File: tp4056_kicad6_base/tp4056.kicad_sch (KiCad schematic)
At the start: 21 parts, among them J1 USB_B_Micro, J2 Conn_01x01_Female, J3 Conn_01x01_Female, J4 Conn_01x01_Female, J5 Conn_01x01_Female, J6 Conn_01x01_Female, J7 Conn_01x01_Female, U1 TP4056, U2 DW01, U3 FS8205A

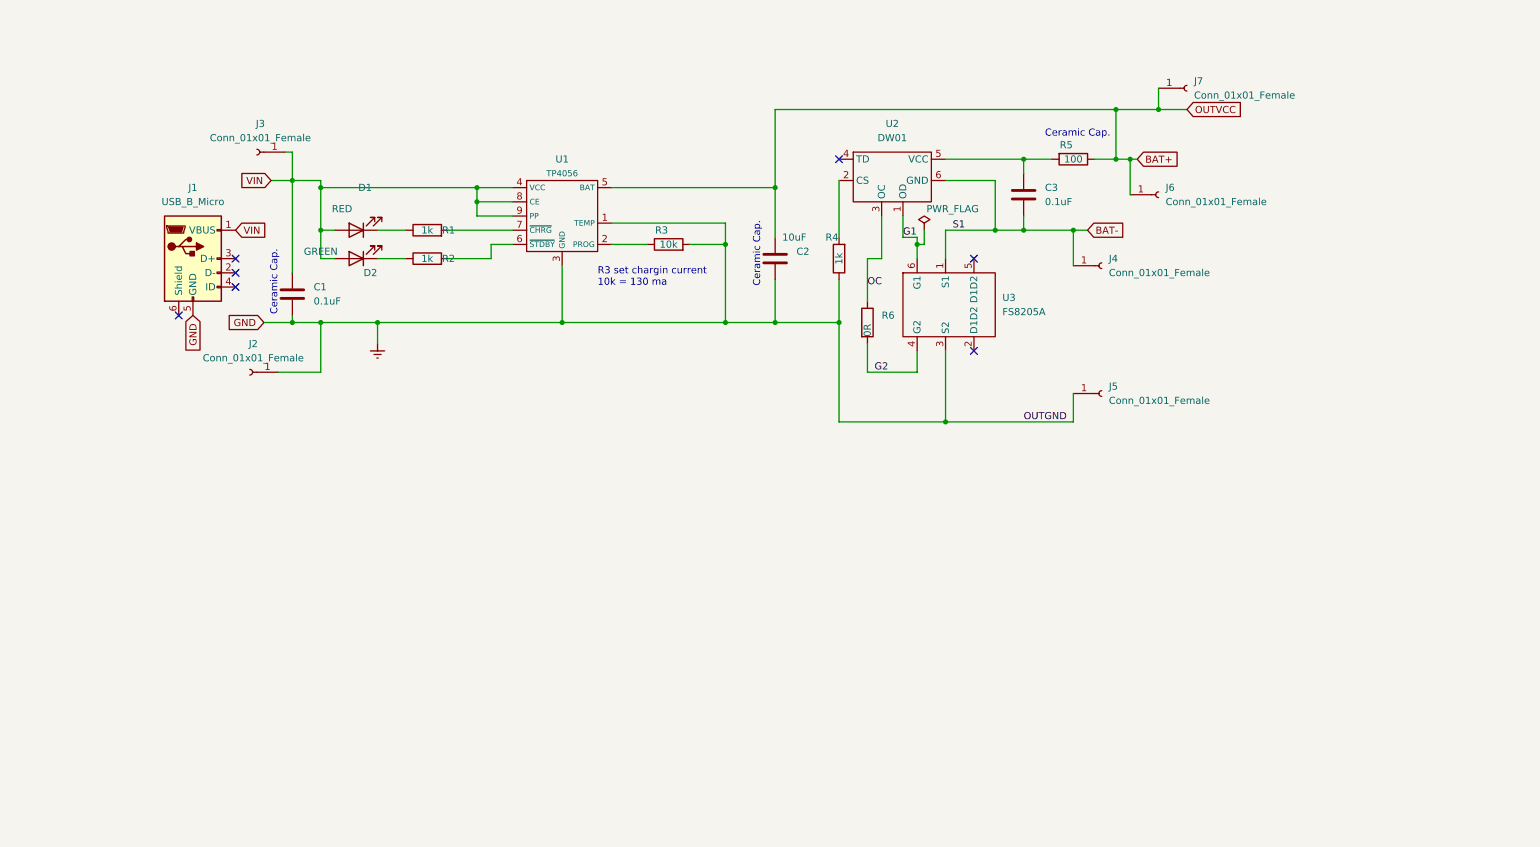
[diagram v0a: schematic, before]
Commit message: redraw and add power path
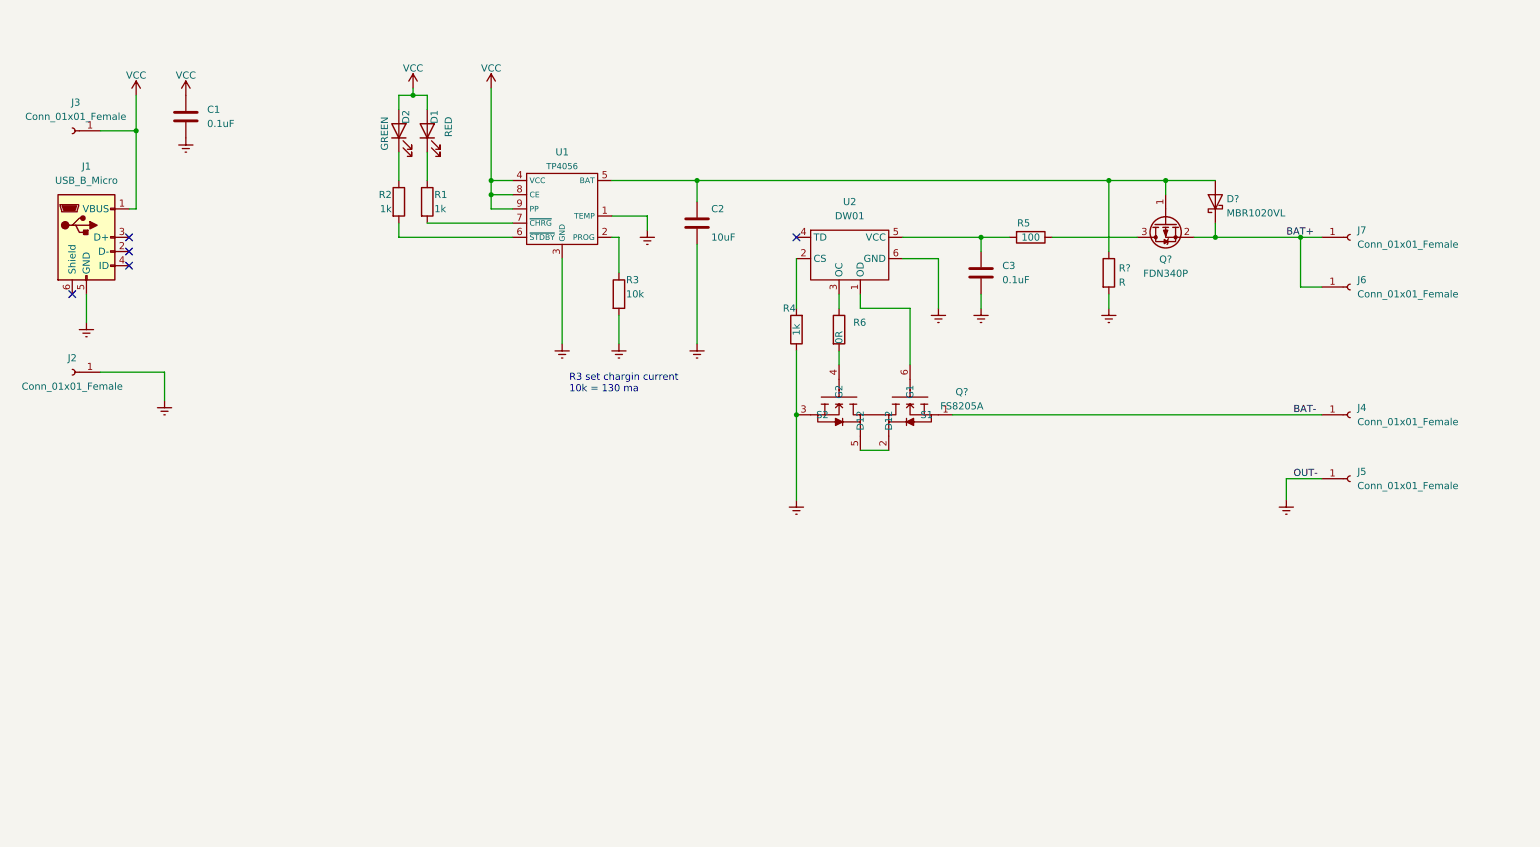
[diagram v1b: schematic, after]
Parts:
- removed U3: FS8205A, Package_TO_SOT_SMD:SOT-23-6_Handsoldering, symbol fs8205:FS8205A
- added D?: MBR1020VL, Diode_SMD:D_SOD-123F, symbol Diode:MBR1020VL
- added Q?: FS8205A, Package_TO_SOT_SMD_AKL:TSOT-23-6_HandSoldering, symbol Tochi:FS8205A
- added Q?: FDN340P, Package_TO_SOT_SMD:SOT-23, symbol Transistor_FET:FDN340P
- added R?: R, symbol Device:R
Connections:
- net BAT+: now also D?.1 (K), Q?.2 (S); no longer C2.1, R5.1, U1.5 (BAT)
- net BAT-: now also Q?.1 (S1); no longer C3.2, U2.6 (GND)
- net Earth: now also C3.2, U2.6 (GND), Q?.3 (S2), R?.2
- net G1: no longer names the net of U2.1 (OD)
- net G1: now also Q?.6 (G1)
- net G2: no longer names the net of R6.2
- net G2: now also Q?.4 (G2)
- net OC: no longer names the net of R6.1, U2.3 (OC)
- net VIN renamed VCC
- new net: C2.1, D?.2 (A), Q?.1 (G), R?.1, U1.5 (BAT)
- new net: Q?.2 (D12), Q?.5 (D12)
- new net: Q?.3 (D), R5.1
- no-connect marks 7 -> 5
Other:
- note removed: "Ceramic Cap."
- moved on the sheet: C1, C2, C3, D1, D2, J1, J2, J3, J4, J5, J6, J7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

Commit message: fix output path
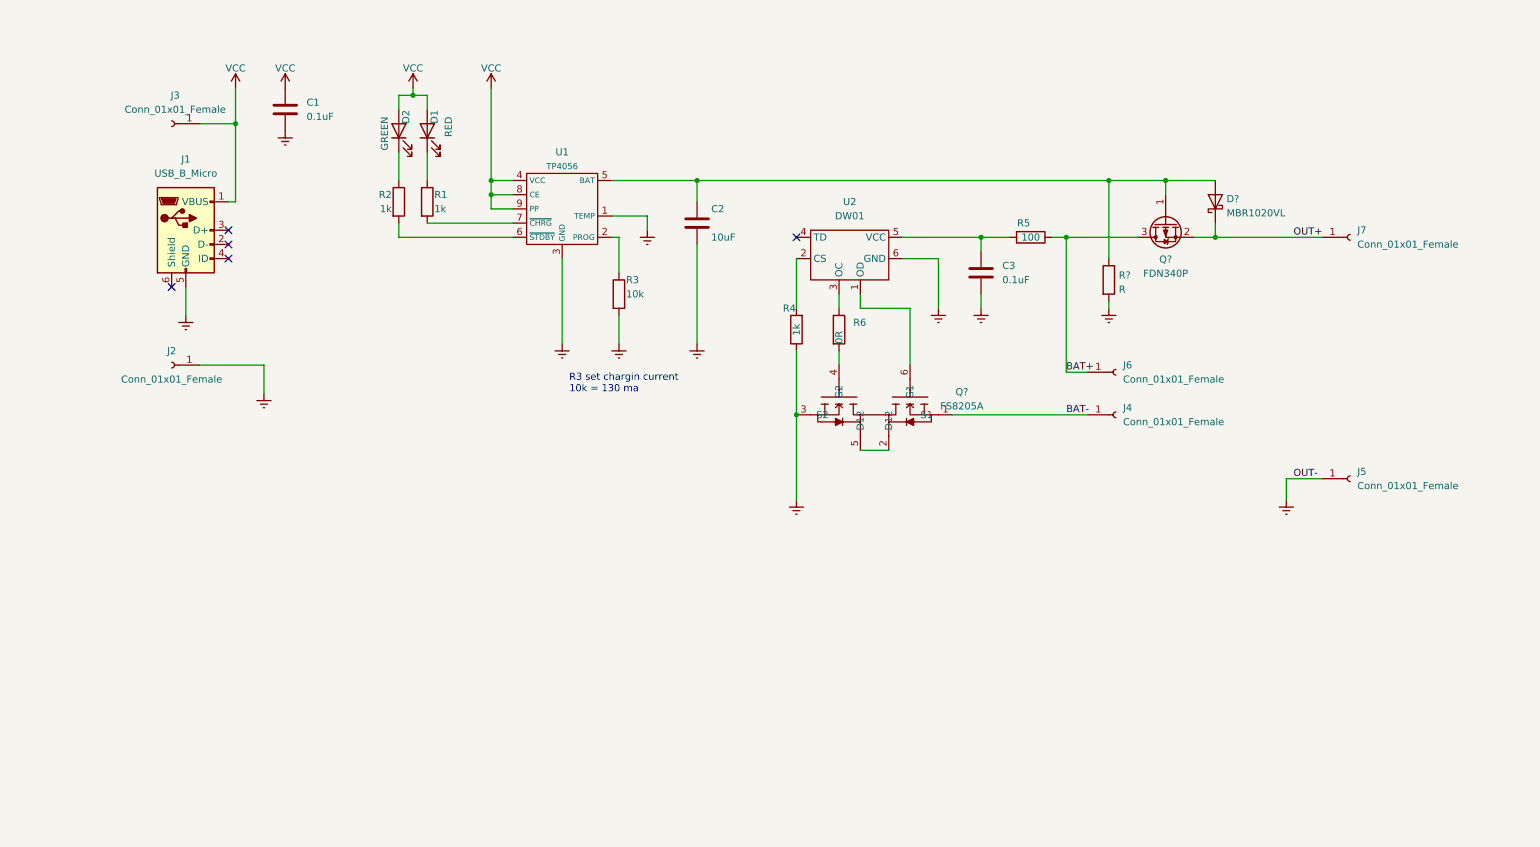
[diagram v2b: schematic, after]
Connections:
- net BAT+: now also Q?.3 (D), R5.1; no longer D?.1 (K), J7.1 (Pin_1), Q?.2 (S)
- new net OUT+: D?.1 (K), J7.1 (Pin_1), Q?.2 (S)
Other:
- title: (none) -> Batery charger w/TP4056, protect and power path
- moved on the sheet: C1, J1, J2, J3, J4, J6, R?

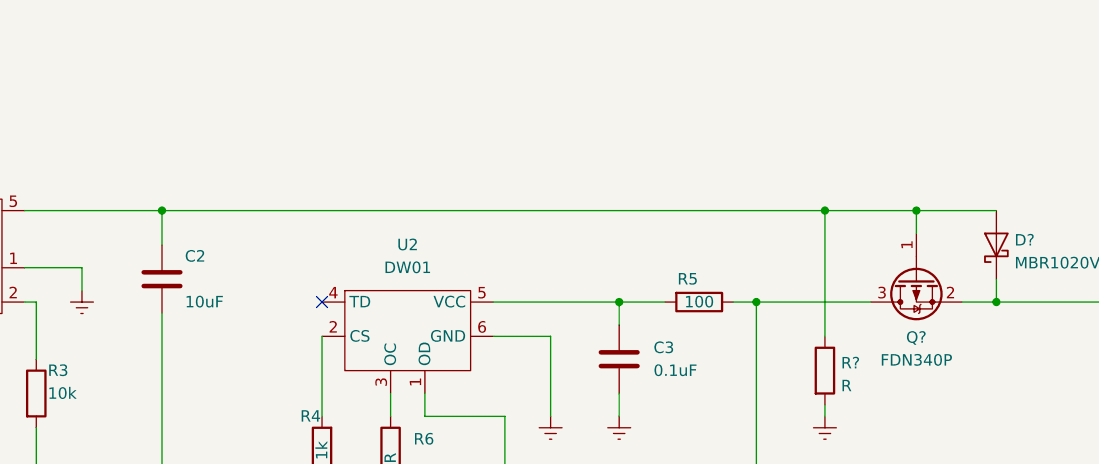
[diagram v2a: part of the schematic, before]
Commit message: fix output path
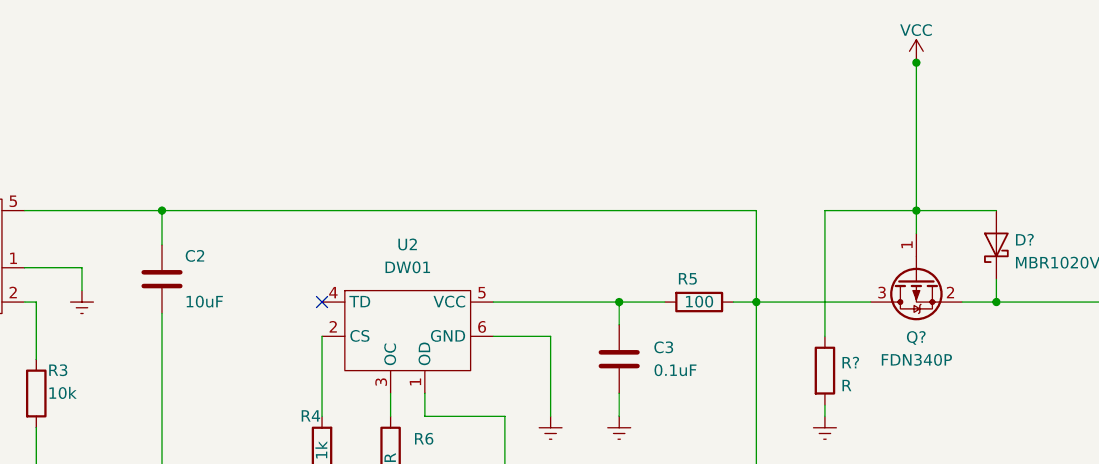
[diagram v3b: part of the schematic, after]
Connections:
- net BAT+: now also C2.1, U1.5 (BAT)
- net VCC: now also D?.2 (A), Q?.1 (G), R?.1
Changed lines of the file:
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@@
   (junction (at 99.06 76.2) (diameter 0) (color 0 0 0 0)
   )
+  (junction (at 135.89 76.2) (diameter 0) (color 0 0 0 0)
+  )
   (junction (at 53.34 66.04) (diameter 0) (color 0 0 0 0)
   )
+  (junction (at 219.71 59.7661) (diameter 0) (color 0 0 0 0)
+  )
   (junction (at 99.06 78.74) (diameter 0) (color 0 0 0 0)
   )
-  (junction (at 209.55 76.2) (diameter 0) (color 0 0 0 0)
-  )
   (junction (at 85.09 60.96) (diameter 0) (color 0 0 0 0)
   )
@@
   )
   (junction (at 228.6 86.36) (diameter 0) (color 0 0 0 0)
-  )
-  (junction (at 135.89 76.2) (diameter 0) (color 0 0 0 0)
   )
   (junction (at 186.69 86.36) (diameter 0) (color 0 0 0 0)
@@
     (stroke (width 0) (type default) (color 0 0 0 0))
   )
+  (wire (pts (xy 135.89 76.2) (xy 201.93 76.2))
+    (stroke (width 0) (type default) (color 0 0 0 0))
+  )
   (wire (pts (xy 153.67 106.68) (xy 153.67 118.11))
     (stroke (width 0) (type default) (color 0 0 0 0))
@@
     (stroke (width 0) (type default) (color 0 0 0 0))
   )
+  (wire (pts (xy 219.71 59.69) (xy 219.71 59.7661))
+    (stroke (width 0) (type default) (color 0 0 0 0))
+  )
   (wire (pts (xy 87.63 60.96) (xy 87.63 63.5))
     (stroke (width 0) (type default) (color 0 0 0 0))
@@
     (stroke (width 0) (type default) (color 0 0 0 0))
   )
-  (wire (pts (xy 135.89 76.2) (xy 209.55 76.2))
-    (stroke (width 0) (type default) (color 0 0 0 0))
-  )
   (wire (pts (xy 46.99 109.22) (xy 58.42 109.22))
     (stroke (width 0) (type default) (color 0 0 0 0))
@@
     (stroke (width 0) (type default) (color 0 0 0 0))
   )
+  (wire (pts (xy 201.93 76.2) (xy 201.93 86.36))
+    (stroke (width 0) (type default) (color 0 0 0 0))
+  )
   (wire (pts (xy 165.1 99.06) (xy 173.99 99.06))
     (stroke (width 0) (type default) (color 0 0 0 0))
@@
   )
   (wire (pts (xy 165.1 99.06) (xy 165.1 96.52))
+    (stroke (width 0) (type default) (color 0 0 0 0))
+  )
+  (wire (pts (xy 219.71 59.7661) (xy 219.71 76.2))
     (stroke (width 0) (type default) (color 0 0 0 0))
   )
@@
     (pin "1")
   )
+  (symbol (lib_id "power:VCC") (at 219.71 59.7661 0) (unit 1)
+    (in_bom yes) (on_board yes)
+    (property "Reference" "#PWR?" (id 0) (at 219.71 63.5761 0)
+      (effects (font (size 1.27 1.27)) hide)
+    )
+    (property "Value" "VCC" (id 1) (at 219.71 56.1903 0))
+    (property "Footprint" "" (id 2) (at 219.71 59.7661 0)
+      (effects (font (size 1.27 1.27)) hide)
+    )
+    (property "Datasheet" "" (id 3) (at 219.71 59.7661 0)
+      (effects (font (size 1.27 1.27)) hide)
+    )
+    (pin "1")
+  )
   (symbol (lib_id "Connector:Conn_01x01_Female") (at 41.91 109.22 180) (unit 1)
     (in_bom yes) (on_board yes)
@@
       (reference "#PWR?") (unit 1) (value "Earth") (footprint "")
     )
+    (path "/ef9b9bd4-6867-4791-b6d5-aa866ff273fa"
+      (reference "#PWR?") (unit 1) (value "VCC") (footprint "")
+    )
     (path "/7870a9db-0a4b-4ce4-a426-dcf645359822"

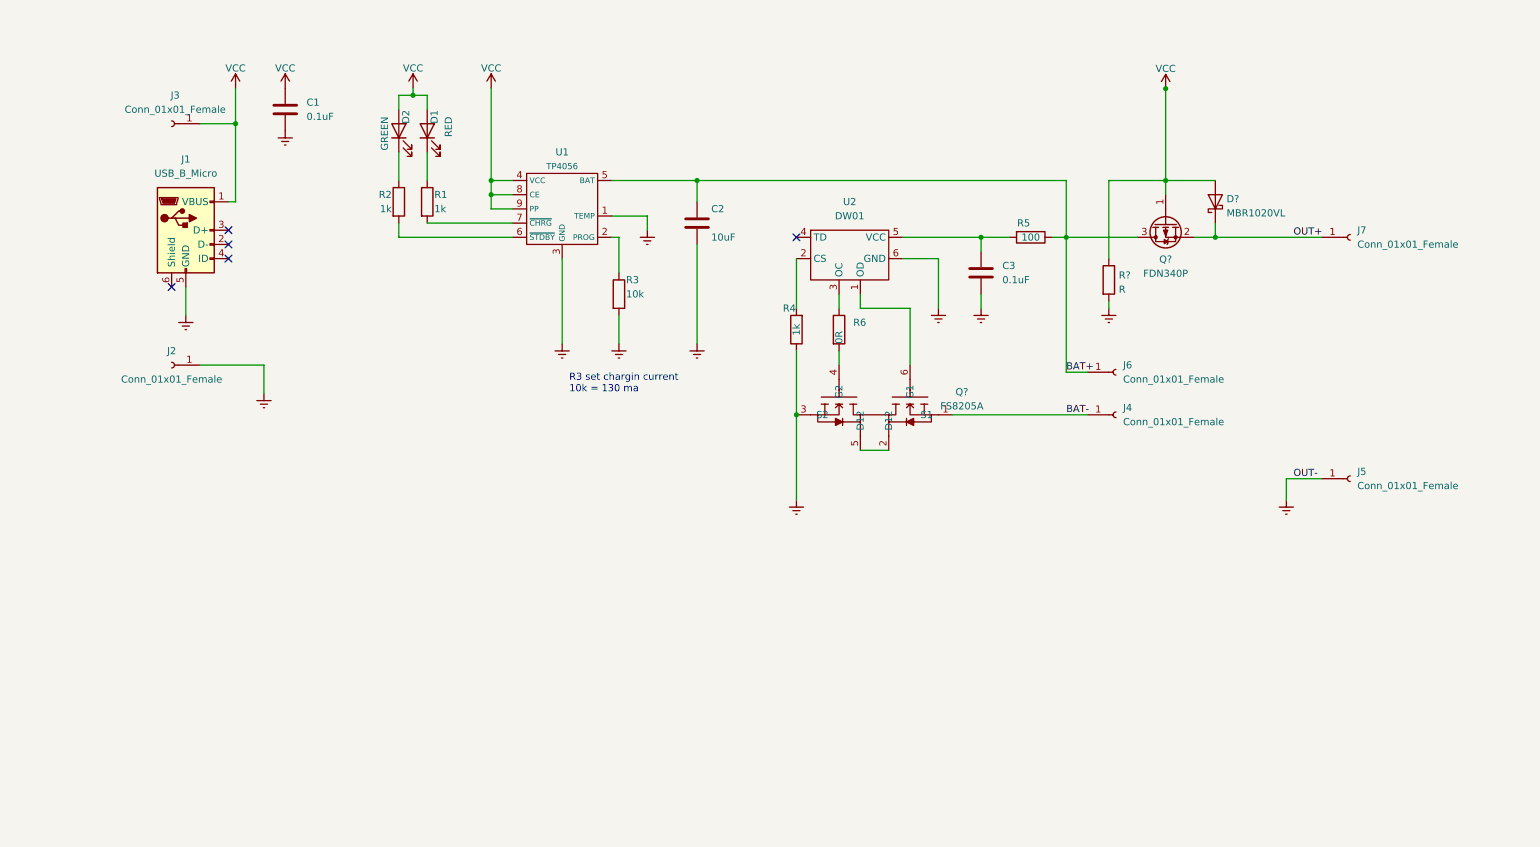
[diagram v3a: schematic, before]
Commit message: add Rprog table
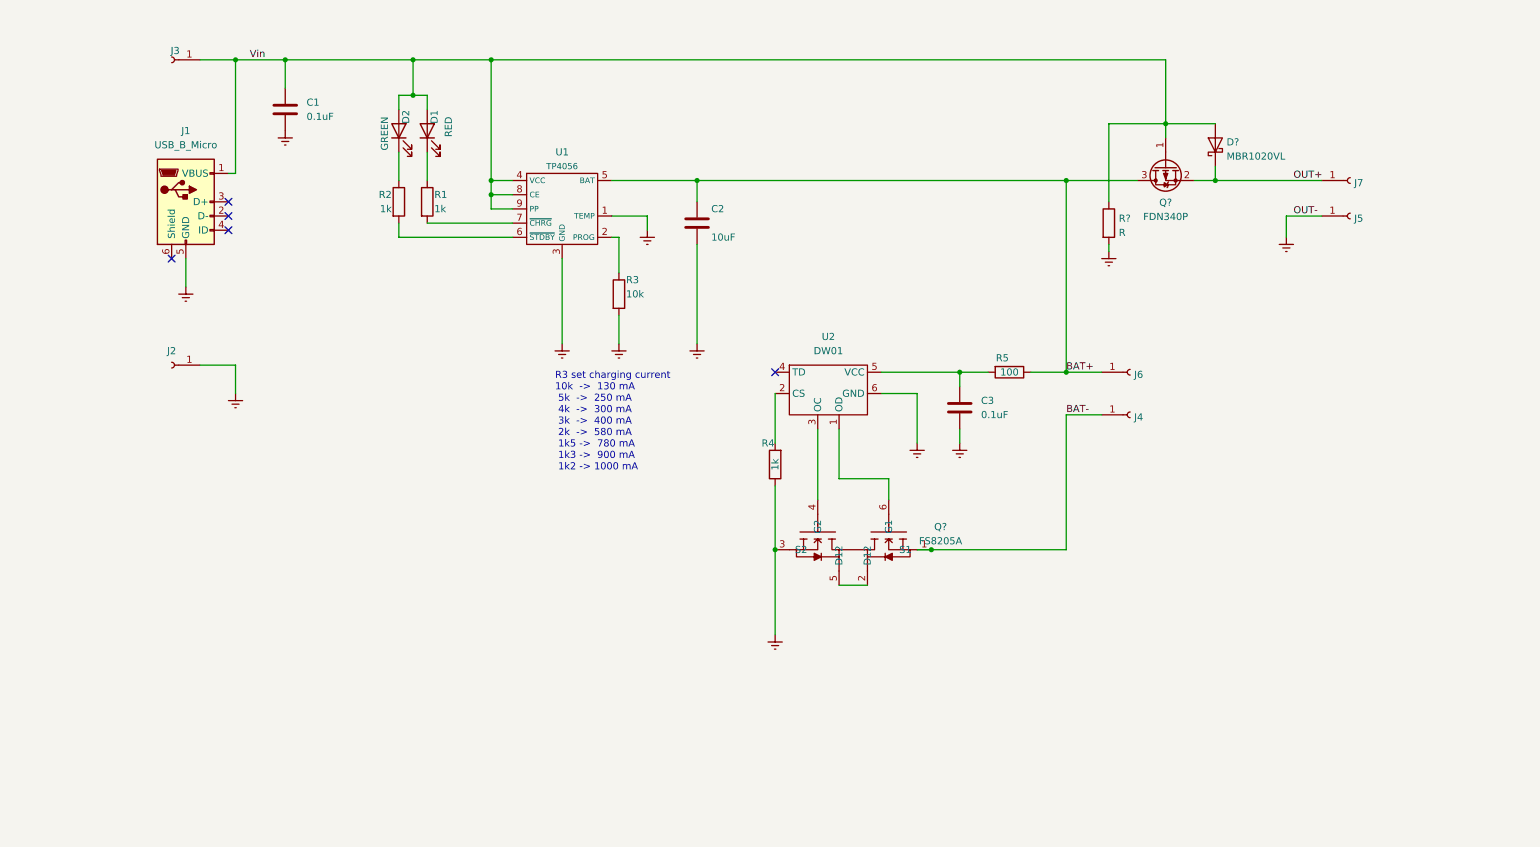
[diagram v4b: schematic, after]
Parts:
- removed R6: 0R, Resistor_SMD:R_1206_3216Metric_Pad1.30x1.75mm_HandSolder, symbol Device:R
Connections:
- net at Q?.4 (G2): now also U2.3 (OC)
- net VCC renamed Vin
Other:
- note added: "R3 set charging current 10k -> 130 mA 5k -> 250 mA 4k -> 300 mA 3k -> 400 mA 2k -> 580 mA 1k5 -> 780 mA 1k3 -> 900 mA 1k2 -> 1000 mA"
- note removed: "R3 set chargin current 10k = 130 ma"
- moved on the sheet: C3, D?, J1, J3, J4, J5, J6, J7, Q?, R4, R5, R?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
